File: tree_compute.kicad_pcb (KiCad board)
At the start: 2 copper layers, 61 x 76.2 mm, 48 parts, among them J1 AVR-ISP-6, U1 ATtiny13A-SSU, U2 ATtiny10-TS

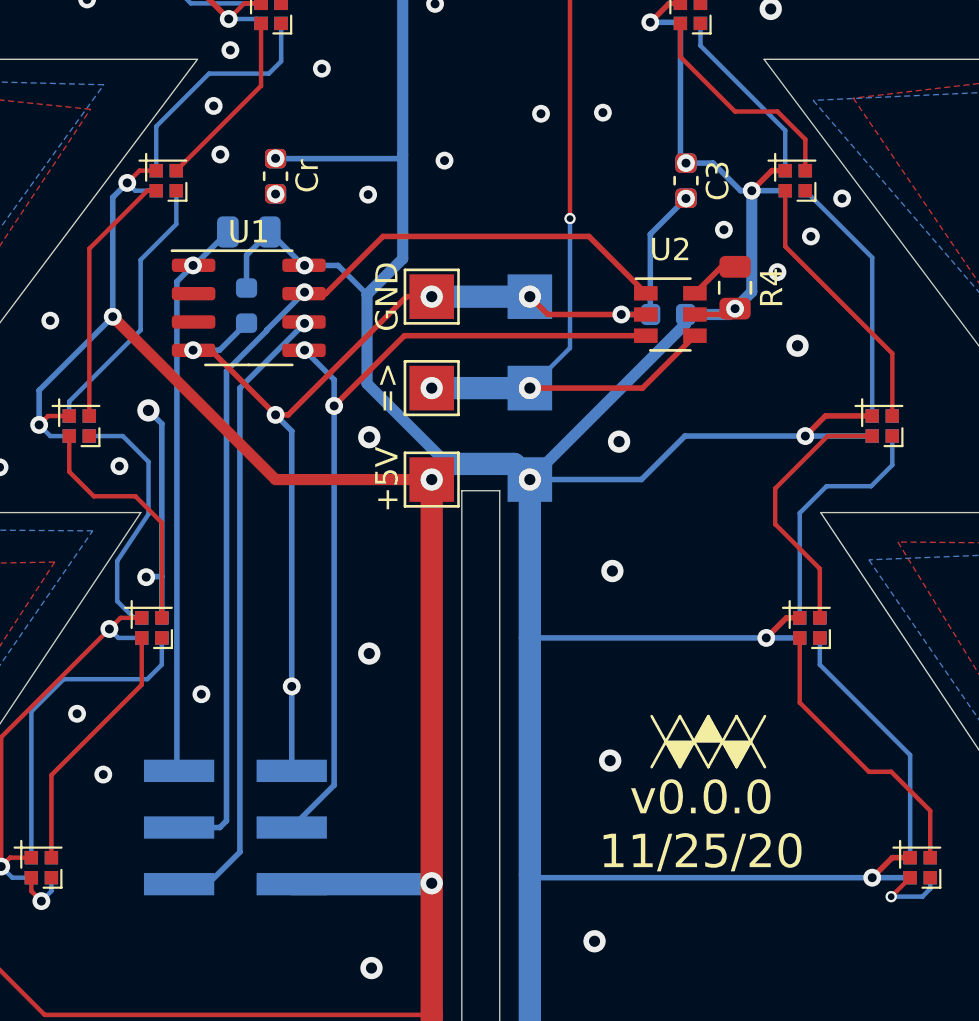
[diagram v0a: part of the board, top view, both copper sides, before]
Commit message: Update with changes to use attiny13a only
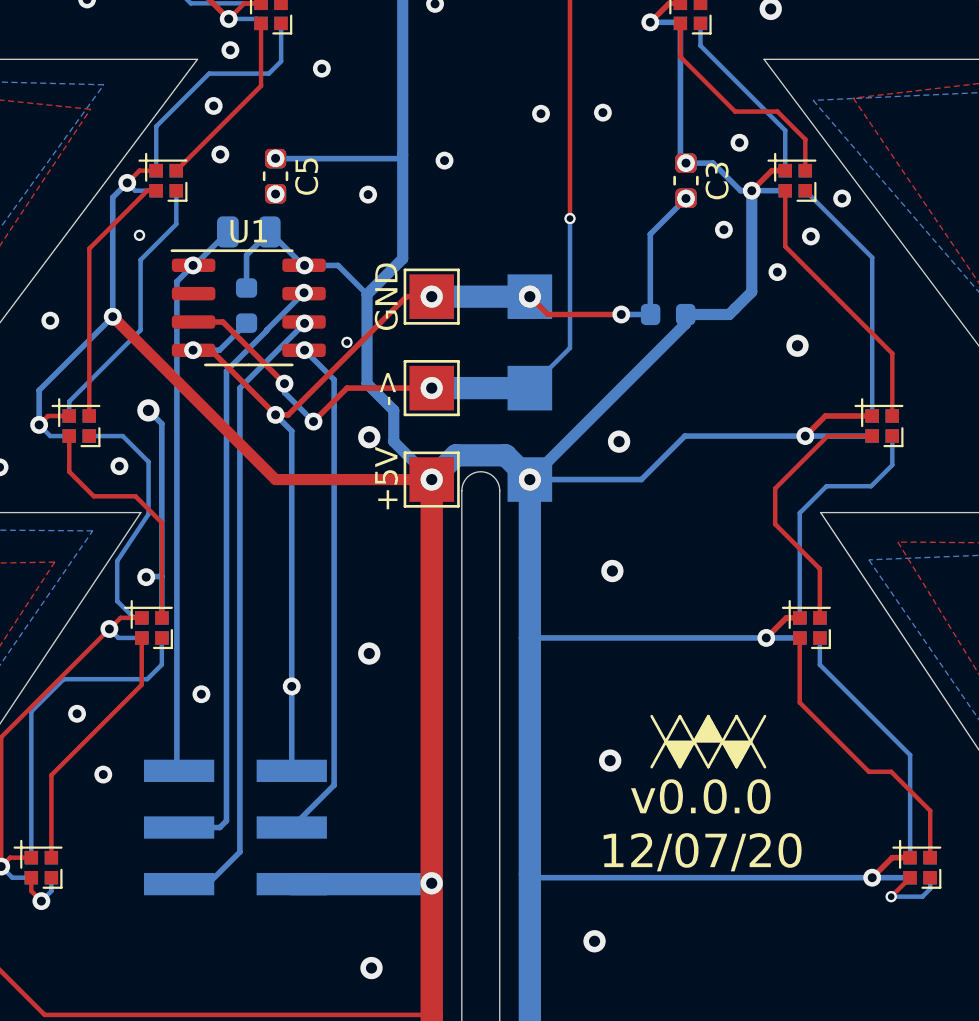
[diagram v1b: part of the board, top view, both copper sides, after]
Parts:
- removed R4: 10kR, Resistor_SMD:R_0805_2012Metric
- removed U2: ATtiny10-TS, Package_TO_SOT_SMD:SOT-23-6
- renumbered => to ->, Cr to C5
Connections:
- U1 pad 3: (no net) -> DOUT
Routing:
- net SCK: track 44.8 -> 27.4 mm
- net MOSI: track 38.0 -> 22.7 mm, vias 2 -> 1
- net DOUT: track 59.4 -> 64.4 mm, vias 3 -> 4
- net Net-(R4-Pad1): track 2.29 -> 0.00 mm
- net +5V: track 350.9 -> 349.7 mm, vias 23 -> 22
- net LGND: track 62.8 -> 61.7 mm, vias 58 -> 61
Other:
- board text added: "v0.0.0 12/07/20"
- board text removed: "v0.0.0 11/25/20"

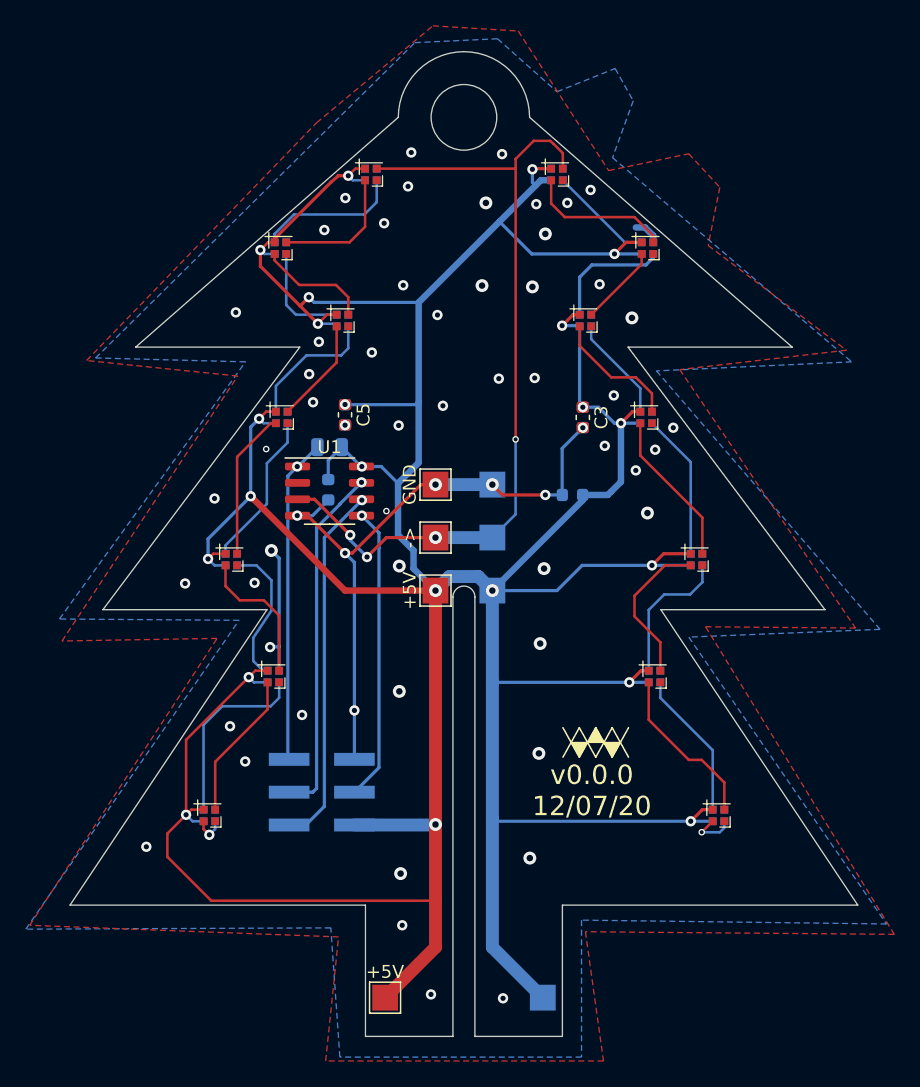
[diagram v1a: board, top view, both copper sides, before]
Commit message: Move right side LEDs to back to break up pattern
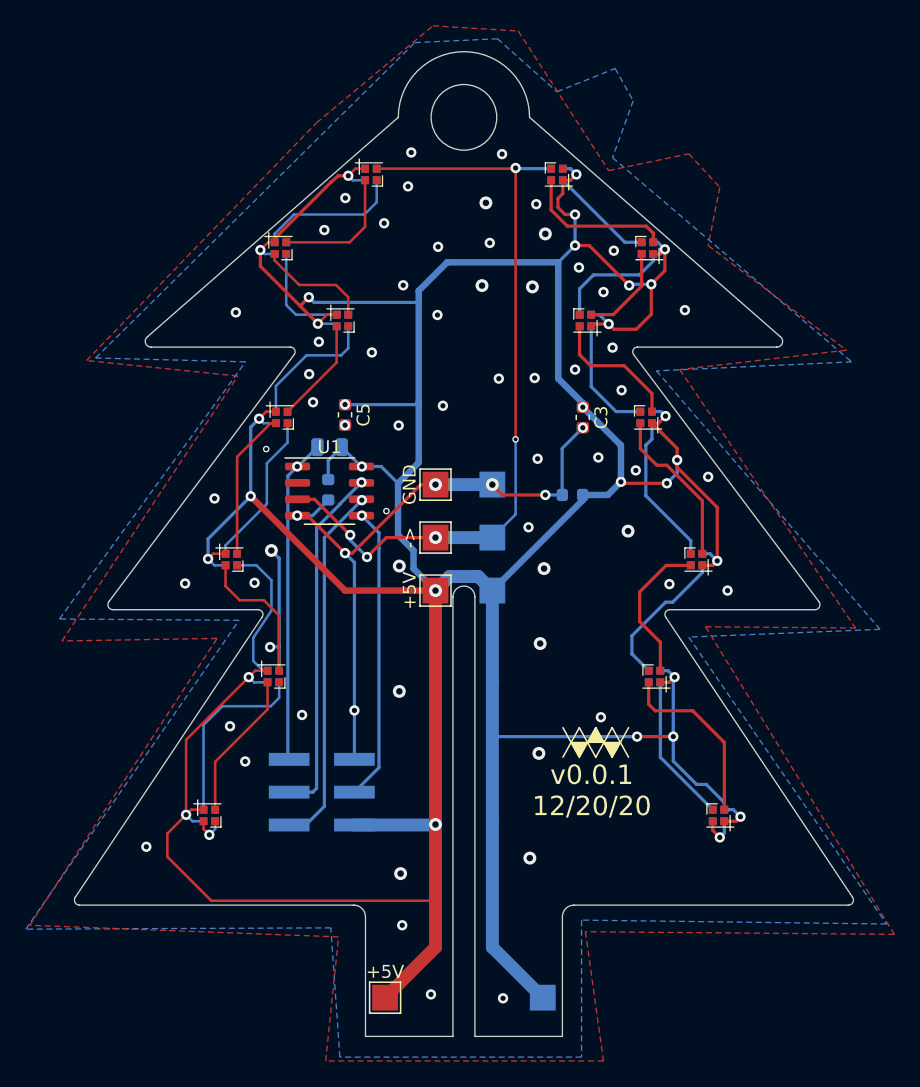
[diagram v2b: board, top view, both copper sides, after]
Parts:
- D1, D2, D3, D4, D5, D6, D7: moved to B.Cu
- D10, D11, D12, D13, D14, D8, D9: moved to F.Cu
- turned D1 to 180 degrees
- turned D10 to 180 degrees
- turned D11 to 180 degrees
- turned D12 to 180 degrees
- turned D13 to 180 degrees
- turned D14 to 180 degrees
- turned D2 to 180 degrees
- turned D3 to 180 degrees
- turned D4 to 180 degrees
- turned D5 to 180 degrees
- turned D6 to 180 degrees
- turned D7 to 180 degrees
- turned D8 to 180 degrees
- turned D9 to 180 degrees
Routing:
- net +5V: track 349.7 -> 364.2 mm, vias 22 -> 30
- net DOUT: track 64.4 -> 60.7 mm, vias 4 -> 5
- net Net-(D13-Pad1): track 8.09 -> 11.6 mm
- net Net-(D1-Pad1): track 11.2 -> 8.09 mm
- net Net-(D2-Pad1): track 6.32 -> 9.14 mm
- net Net-(D8-Pad1): track 11.5 -> 14.0 mm
- net Net-(D11-Pad1): track 8.17 -> 10.4 mm
- net Net-(D12-Pad1): track 9.51 -> 7.31 mm
- net LGND: track 61.7 -> 59.5 mm, vias 61 -> 69
- net Net-(D6-Pad1): track 12.9 -> 11.5 mm
- net Net-(D10-Pad1): track 11.3 -> 12.5 mm
- net Net-(D3-Pad1): track 10.0 -> 9.27 mm
- net Net-(D7-Pad1): track 3.60 -> 2.87 mm
- net Net-(D5-Pad1): track 12.0 -> 11.3 mm
- net Net-(D10-Pad3): track 11.0 -> 11.6 mm
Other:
- board size 61 x 76.2 mm -> 60.3 x 76.2 mm
- board text added: "v0.0.1 12/20/20"
- board text removed: "v0.0.0 12/07/20"
